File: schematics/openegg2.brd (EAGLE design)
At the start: 89.8 x 34.8 mm, 69 parts, among them IC1 L5973D, IC2 ZLDO330, J1 22-27-2031-03, Q1 BC846, Q2 BC846, Q3 BC846, Q4 BC846, Q6 BC856, Q8 BC846, X2 32.768KHz

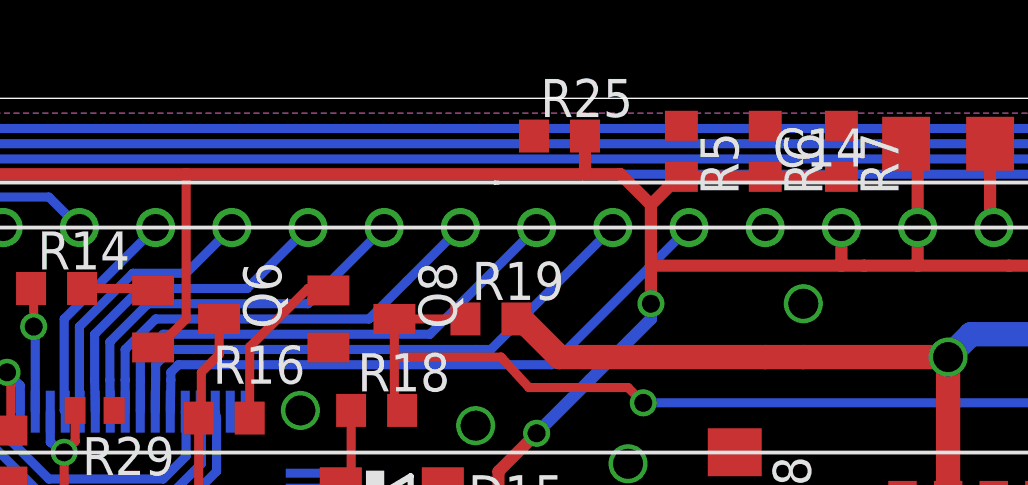
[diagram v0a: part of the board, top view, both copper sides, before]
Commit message: Improve step down converter design for GSM module power.
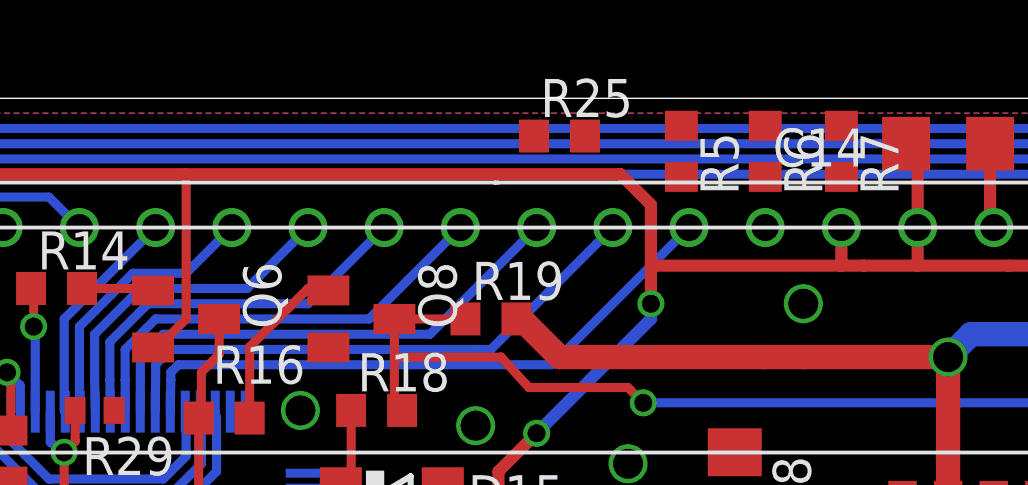
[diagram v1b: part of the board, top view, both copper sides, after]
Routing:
- net +3V3: track 212.8 -> 204.8 mm
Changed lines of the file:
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@@
 <wire x1="3.81" y1="31.242" x2="4.826" y2="32.258" width="0.4064" layer="1"/>
 <wire x1="4.826" y1="32.258" x2="17.526" y2="32.258" width="0.4064" layer="1"/>
-<wire x1="17.526" y1="32.258" x2="30.734" y2="32.258" width="0.4064" layer="1"/>
-<wire x1="30.734" y1="32.258" x2="32.004" y2="32.258" width="0.4064" layer="1"/>
+<wire x1="17.526" y1="32.258" x2="32.004" y2="32.258" width="0.4064" layer="1"/>
 <wire x1="32.004" y1="32.258" x2="33.02" y2="31.242" width="0.4064" layer="1"/>
 <wire x1="40.132" y1="29.21" x2="41.91" y2="29.21" width="0.4064" layer="1"/>
@@
 <contactref element="R6" pad="2"/>
 <contactref element="R5" pad="2"/>
-<wire x1="34.036" y1="32.17" x2="33.948" y2="32.17" width="0.4064" layer="1"/>
-<wire x1="33.948" y1="32.17" x2="33.02" y2="31.242" width="0.4064" layer="1"/>
-<wire x1="36.83" y1="32.17" x2="34.036" y2="32.17" width="0.4064" layer="1"/>
-<wire x1="39.37" y1="32.17" x2="36.83" y2="32.17" width="0.4064" layer="1"/>
-<wire x1="30.822" y1="33.528" x2="30.822" y2="32.346" width="0.4064" layer="1"/>
-<wire x1="30.822" y1="32.346" x2="30.734" y2="32.258" width="0.4064" layer="1"/>
+<wire x1="39.37" y1="32.17" x2="30.822" y2="33.528" width="0" layer="19" extent="1-1"/>
+<wire x1="36.83" y1="32.17" x2="39.37" y2="32.17" width="0" layer="19" extent="1-1"/>
+<wire x1="34.036" y1="32.17" x2="36.83" y2="32.17" width="0" layer="19" extent="1-1"/>
+<wire x1="6.35" y1="0.762" x2="34.036" y2="32.17" width="0" layer="19" extent="1-1"/>
 </signal>
 <signal name="N$27">

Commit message: Undo wrong checkin
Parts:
- removed L4: 1uH, rcl:L1812
- added C15: 100uF, rcl:153CLV-0505
- added F2: 3A, rcl:R2010
- added VR2: 4.5V, varistor:CT/CN1812
- C2: value 100uF -> 10uF ceramic; device rcl:140CLH-1014 -> rcl:C1210K
- C9: value 30uF -> 470uF; device rcl:140CLH-1014 -> rcl:CT7343
- VR1: device varistor:CT/CN1206 -> rcl:R2010
- moved VR1 8.29 mm to (71.1, 26.4)
- moved C2 4.32 mm to (71.1, 22.6), turned to 180 degrees
- moved C9 3.06 mm to (84.8, 25.1), turned to 90 degrees
- moved F1 0.25 mm to (60.7, 21.8)
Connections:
- net +12V: now also C15.+, C2.1; no longer C2.+
- net GND: now also C15.-, C2.2, VR2.1; no longer C2.-
- net N$13: now also F2.1; no longer L4.2
- net V+: now also F2.2, VR2.2; no longer L4.1
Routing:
- net +12V: track 81.9 -> 77.4 mm
- net N$13: track 38.7 -> 39.9 mm
- net V+: track 26.5 -> 27.6 mm
- net GND: vias 46 -> 47

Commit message: Route button pull up resistors.
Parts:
- removed R25, R5, R6, R7: 10k, rcl:R0603
- added RN1: (no value), resistor-array:742-8
- moved R14 0.51 mm to (13.2, 27.9)
- moved R18 0.25 mm to (23.9, 24.1)
- moved Q6 0.25 mm to (17.5, 27.2)
- moved Q8 0.25 mm to (23.4, 27.2)
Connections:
- net +3V3: now also RN1.5, RN1.6, RN1.7, RN1.8; no longer R25.2, R5.2, R6.2, R7.2
- net B0: now also RN1.2; no longer R25.1
- net B1: now also RN1.1; no longer R7.1
- net B2: now also RN1.4; no longer R6.1
- net B3: now also RN1.3; no longer R5.1
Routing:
- net B0: track 98.5 -> 106.8 mm, vias 1 -> 2
- net B2: track 131.7 -> 136.3 mm, vias 0 -> 1
- net B1: track 73.8 -> 77.2 mm, vias 0 -> 1
- net B3: track 98.2 -> 101.0 mm, vias 0 -> 1
- net +3V3: track 204.8 -> 205.7 mm
